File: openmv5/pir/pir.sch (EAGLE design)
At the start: 56 parts, among them IC1 AP3032KTR-G1, IC2 AP3032KTR-G1, J1 OPENMV5-TOP, Q1 2N7002KW_R1_00001, U1 EKMB1307113K, U2 MIC5365-3.3YMT-TZ

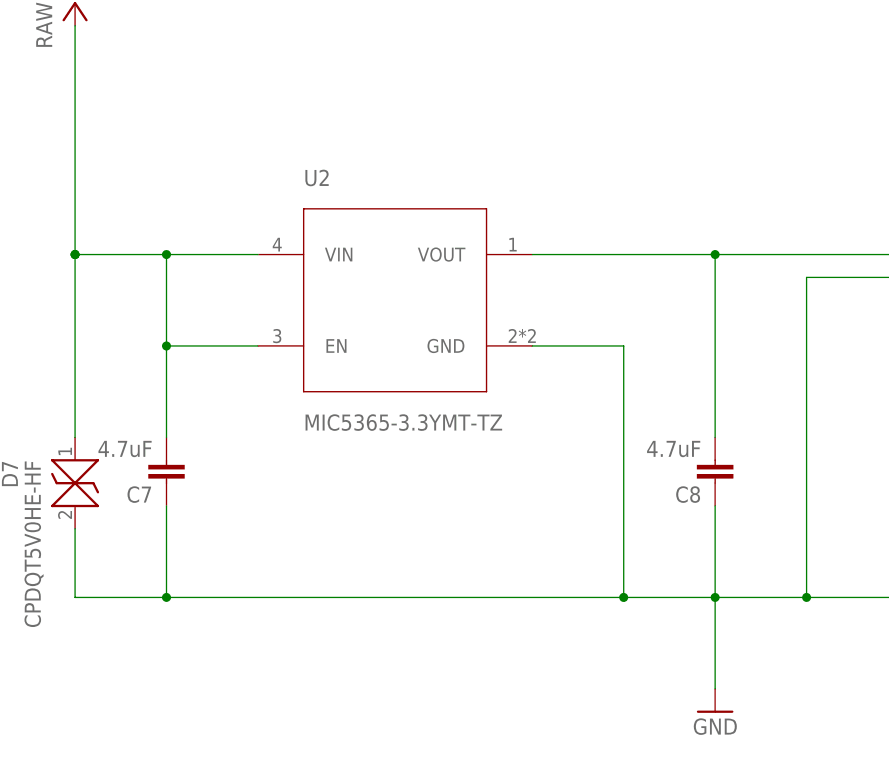
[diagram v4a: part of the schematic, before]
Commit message: Final PIR shield, fixed regulator
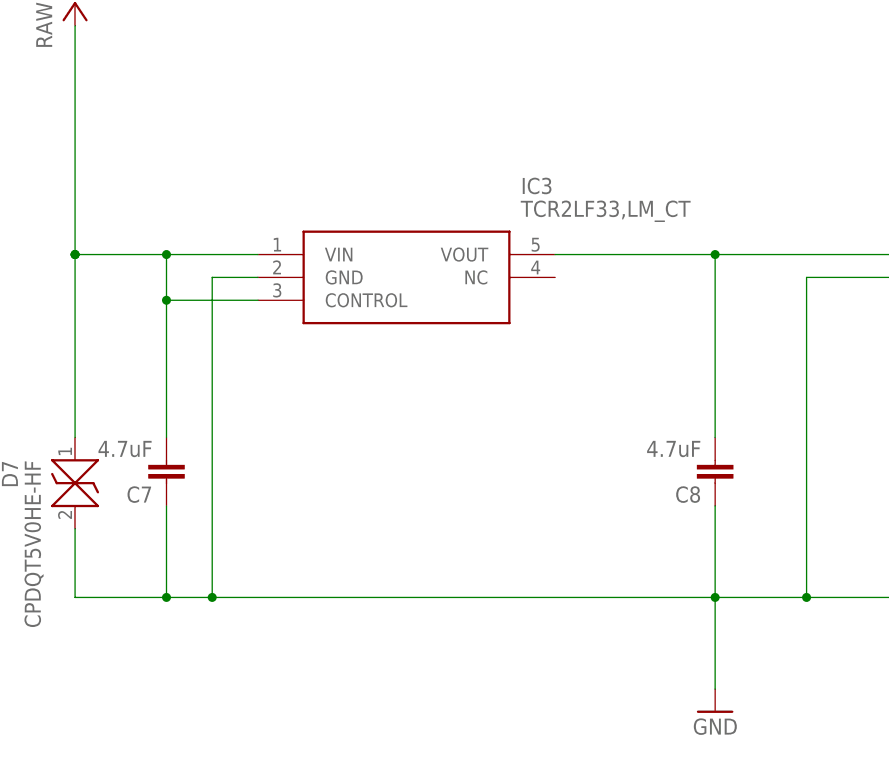
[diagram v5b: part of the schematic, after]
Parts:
- removed U2: MIC5365-3.3YMT-TZ, MIC5365-3.3YMT-TZ:MIC5365-3.3YMT-TZ
- added IC3: TCR2LF33,LM_CT, TCR2LF33_LM_CT:TCR2LF33,LM_CT
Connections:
- net GND: now also IC3.GND; no longer U2.GND
- net RAW: now also IC3.CONTROL, IC3.VIN; no longer U2.EN, U2.VIN
- net VDD: now also IC3.VOUT; no longer U2.VOUT
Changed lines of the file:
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@@
 <attribute name="MPN" value="JMK105BBJ475MV-F"/>
-</part>
-<part name="U2" library="MIC5365-3.3YMT-TZ" deviceset="MIC5365-3.3YMT-TZ" device="">
-<attribute name="MPN" value="MIC5365-3.3YMT-TZ"/>
 </part>
 <part name="R5" library="sfe" deviceset="RESISTOR" device="0402-RES" value="1K">
@@
 <part name="JP2" library="SparkFun-Jumpers" library_urn="urn:adsk.eagle:library:528" deviceset="JUMPER-SMT_2_NC_PASTE" device="_SILK" package3d_urn="urn:adsk.eagle:package:39282/1"/>
 <part name="JP3" library="SparkFun-Jumpers" library_urn="urn:adsk.eagle:library:528" deviceset="JUMPER-SMT_2_NC_PASTE" device="_SILK" package3d_urn="urn:adsk.eagle:package:39282/1"/>
+<part name="IC3" library="TCR2LF33_LM_CT" deviceset="TCR2LF33,LM_CT" device="">
+<attribute name="MPN" value="TC7SZ07FU,LJ(CT"/>
+</part>
 </parts>
 <sheets>
@@
 <attribute name="MPN" x="27.94" y="78.74" size="1.778" layer="96" rot="R180" display="off"/>
 </instance>
-<instance part="U2" gate="G$1" x="53.34" y="96.52" smashed="yes">
-<attribute name="NAME" x="43.18" y="109.22" size="1.778" layer="95"/>
-<attribute name="VALUE" x="43.18" y="83.82" size="1.778" layer="96" rot="MR180"/>
-<attribute name="MPN" x="53.34" y="96.52" size="1.778" layer="96" display="off"/>
-</instance>
 <instance part="R5" gate="G$1" x="162.56" y="119.38" smashed="yes" rot="R90">
 <attribute name="MPN" x="162.56" y="119.38" size="1.778" layer="96" rot="R90" display="off"/>
@@
 <attribute name="NAME" x="302.26" y="91.44" size="1.778" layer="95" font="vector"/>
 <attribute name="VALUE" x="302.26" y="86.36" size="1.778" layer="96" font="vector" align="top-left"/>
+</instance>
+<instance part="IC3" gate="G$1" x="38.1" y="101.6" smashed="yes">
+<attribute name="NAME" x="67.31" y="109.22" size="1.778" layer="95" align="center-left"/>
+<attribute name="VALUE" x="67.31" y="106.68" size="1.778" layer="96" align="center-left"/>
+<attribute name="MPN" x="38.1" y="101.6" size="1.778" layer="96" display="off"/>
 </instance>
 </instances>
@@
 <pinref part="C7" gate="G$1" pin="1"/>
 <wire x1="27.94" y1="73.66" x2="27.94" y2="63.5" width="0.1524" layer="91"/>
-<wire x1="27.94" y1="63.5" x2="78.74" y2="63.5" width="0.1524" layer="91"/>
-<wire x1="68.58" y1="91.44" x2="78.74" y2="91.44" width="0.1524" layer="91"/>
-<wire x1="78.74" y1="91.44" x2="78.74" y2="63.5" width="0.1524" layer="91"/>
-<wire x1="78.74" y1="63.5" x2="88.9" y2="63.5" width="0.1524" layer="91"/>
+<wire x1="27.94" y1="63.5" x2="33.02" y2="63.5" width="0.1524" layer="91"/>
+<wire x1="33.02" y1="63.5" x2="88.9" y2="63.5" width="0.1524" layer="91"/>
 <pinref part="C8" gate="G$1" pin="1"/>
 <wire x1="88.9" y1="63.5" x2="88.9" y2="73.66" width="0.1524" layer="91"/>
@@
 <junction x="88.9" y="63.5"/>
 <pinref part="GND7" gate="1" pin="GND"/>
-<junction x="78.74" y="63.5"/>
-<pinref part="U2" gate="G$1" pin="GND"/>
 <pinref part="U1" gate="G$1" pin="GND"/>
 <wire x1="109.22" y1="99.06" x2="99.06" y2="99.06" width="0.1524" layer="91"/>
@@
 <wire x1="17.78" y1="63.5" x2="27.94" y2="63.5" width="0.1524" layer="91"/>
 <junction x="27.94" y="63.5"/>
+<pinref part="IC3" gate="G$1" pin="GND"/>
+<wire x1="38.1" y1="99.06" x2="33.02" y2="99.06" width="0.1524" layer="91"/>
+<wire x1="33.02" y1="99.06" x2="33.02" y2="63.5" width="0.1524" layer="91"/>
+<junction x="33.02" y="63.5"/>
 </segment>
 <segment>
@@
 <wire x1="17.78" y1="101.6" x2="27.94" y2="101.6" width="0.1524" layer="91"/>
 <wire x1="27.94" y1="101.6" x2="38.1" y2="101.6" width="0.1524" layer="91"/>
-<wire x1="38.1" y1="91.44" x2="27.94" y2="91.44" width="0.1524" layer="91"/>
+<wire x1="38.1" y1="96.52" x2="27.94" y2="96.52" width="0.1524" layer="91"/>
 <junction x="17.78" y="101.6"/>
 <pinref part="RAW5" gate="G$1" pin="RAW"/>
 <pinref part="C7" gate="G$1" pin="2"/>
-<wire x1="27.94" y1="91.44" x2="27.94" y2="81.28" width="0.1524" layer="91"/>
-<junction x="27.94" y="91.44"/>
-<pinref part="U2" gate="G$1" pin="VIN"/>
-<pinref part="U2" gate="G$1" pin="EN"/>
+<wire x1="27.94" y1="96.52" x2="27.94" y2="81.28" width="0.1524" layer="91"/>
+<junction x="27.94" y="96.52"/>
 <pinref part="D7" gate="G$1" pin="1"/>
 <wire x1="17.78" y1="81.28" x2="17.78" y2="101.6" width="0.1524" layer="91"/>
 <junction x="17.78" y="101.6"/>
-<wire x1="27.94" y1="91.44" x2="27.94" y2="101.6" width="0.1524" layer="91"/>
+<wire x1="27.94" y1="96.52" x2="27.94" y2="101.6" width="0.1524" layer="91"/>
 <junction x="27.94" y="101.6"/>
+<pinref part="IC3" gate="G$1" pin="VIN"/>
+<pinref part="IC3" gate="G$1" pin="CONTROL"/>
 </segment>
 <segment>
@@
 <net name="VDD" class="3">
 <segment>
-<wire x1="68.58" y1="101.6" x2="88.9" y2="101.6" width="0.1524" layer="91"/>
+<wire x1="71.12" y1="101.6" x2="88.9" y2="101.6" width="0.1524" layer="91"/>
 <wire x1="88.9" y1="101.6" x2="88.9" y2="81.28" width="0.1524" layer="91"/>
 <pinref part="C8" gate="G$1" pin="2"/>
-<pinref part="U2" gate="G$1" pin="VOUT"/>
 <wire x1="88.9" y1="101.6" x2="109.22" y2="101.6" width="0.1524" layer="91"/>
 <junction x="88.9" y="101.6"/>
 <pinref part="U1" gate="G$1" pin="VDD"/>
+<pinref part="IC3" gate="G$1" pin="VOUT"/>
 </segment>
 </net>

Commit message: Add more options
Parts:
- added JP4: JUMPER-SMT_2_NO_SILK, SparkFun-Jumpers:JUMPER-SMT_2_NO_SILK
- R5: value 1K -> 100K; MPN CRCW04021K00FKEDC -> AC0402FR-07100KL
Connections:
- new net P11_WAKEUP_INT_2: J1.P9/PWM, JP4.1
- net P11_WAKEUP: now also JP4.2
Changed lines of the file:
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@@
 <attribute name="MPN" value="JMK105BBJ475MV-F"/>
 </part>
-<part name="R5" library="sfe" deviceset="RESISTOR" device="0402-RES" value="1K">
-<attribute name="MPN" value="CRCW04021K00FKEDC"/>
+<part name="R5" library="sfe" deviceset="RESISTOR" device="0402-RES" value="100K">
+<attribute name="MPN" value="AC0402FR-07100KL"/>
 </part>
 <part name="RAW1" library="supply" deviceset="RAW" device="" value="RAW"/>
@@
 <attribute name="MPN" value="TC7SZ07FU,LJ(CT"/>
 </part>
+<part name="JP4" library="SparkFun-Jumpers" library_urn="urn:adsk.eagle:library:528" deviceset="JUMPER-SMT_2_NO" device="_SILK" package3d_urn="urn:adsk.eagle:package:39279/1"/>
 </parts>
 <sheets>
@@
 <attribute name="VALUE" x="67.31" y="106.68" size="1.778" layer="96" align="center-left"/>
 <attribute name="MPN" x="38.1" y="101.6" size="1.778" layer="96" display="off"/>
+</instance>
+<instance part="JP4" gate="G$1" x="304.8" y="93.98" smashed="yes">
+<attribute name="NAME" x="302.26" y="96.52" size="1.778" layer="95" font="vector"/>
+<attribute name="VALUE" x="302.26" y="91.44" size="1.778" layer="96" font="vector" align="top-left"/>
 </instance>
 </instances>
@@
 </segment>
 <segment>
-<wire x1="309.88" y1="88.9" x2="335.28" y2="88.9" width="0.1524" layer="91"/>
+<wire x1="309.88" y1="88.9" x2="320.04" y2="88.9" width="0.1524" layer="91"/>
 <pinref part="JP3" gate="G$1" pin="2"/>
 <label x="314.96" y="88.9" size="1.778" layer="95"/>
+<pinref part="JP4" gate="G$1" pin="2"/>
+<wire x1="320.04" y1="88.9" x2="335.28" y2="88.9" width="0.1524" layer="91"/>
+<wire x1="309.88" y1="93.98" x2="320.04" y2="93.98" width="0.1524" layer="91"/>
+<wire x1="320.04" y1="93.98" x2="320.04" y2="88.9" width="0.1524" layer="91"/>
+<junction x="320.04" y="88.9"/>
 </segment>
 </net>
@@
 </segment>
 </net>
+<net name="P11_WAKEUP_INT_2" class="4">
+<segment>
+<pinref part="J1" gate="G$1" pin="P9/PWM"/>
+<pinref part="JP4" gate="G$1" pin="1"/>
+<wire x1="294.64" y1="93.98" x2="299.72" y2="93.98" width="0.1524" layer="91"/>
+</segment>
+</net>

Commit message: Fix wrong regulator MPN
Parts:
- IC3: MPN TC7SZ07FU,LJ(CT -> TCR2LF33,LM(CT
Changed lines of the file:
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@@
 <part name="JP3" library="SparkFun-Jumpers" library_urn="urn:adsk.eagle:library:528" deviceset="JUMPER-SMT_2_NC_PASTE" device="_SILK" package3d_urn="urn:adsk.eagle:package:39282/1"/>
 <part name="IC3" library="TCR2LF33_LM_CT" deviceset="TCR2LF33,LM_CT" device="">
-<attribute name="MPN" value="TC7SZ07FU,LJ(CT"/>
+<attribute name="MPN" value="TCR2LF33,LM(CT"/>
 </part>
 <part name="JP4" library="SparkFun-Jumpers" library_urn="urn:adsk.eagle:library:528" deviceset="JUMPER-SMT_2_NO" device="_SILK" package3d_urn="urn:adsk.eagle:package:39279/1"/>

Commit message: Update cap value
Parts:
- C3, C6: MPN GRM155R61H105KE05D -> GRM155R6YA105KE11D
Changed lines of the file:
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@@
 </part>
 <part name="C3" library="sfe" deviceset="CAP" device="0402-CAP" value="1uF">
-<attribute name="MPN" value="GRM155R61H105KE05D"/>
+<attribute name="MPN" value="GRM155R6YA105KE11D"/>
 </part>
 <part name="GND1" library="sfe" deviceset="GND" device=""/>
@@
 </part>
 <part name="C6" library="sfe" deviceset="CAP" device="0402-CAP" value="1uF">
-<attribute name="MPN" value="GRM155R61H105KE05D"/>
+<attribute name="MPN" value="GRM155R6YA105KE11D"/>
 </part>
 <part name="GND3" library="sfe" deviceset="GND" device=""/>
